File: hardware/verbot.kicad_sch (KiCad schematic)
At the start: 9 parts, among them J1 Raspberry Pi Zero 2 W, J2 5V USB power bank, M1 Pimoroni OnOff SHIM, M2 DRV8833 carrier, M3 Verbot 3V motor, M4 Verbot gearbox harness, M5 MAX98357A I2S DAC

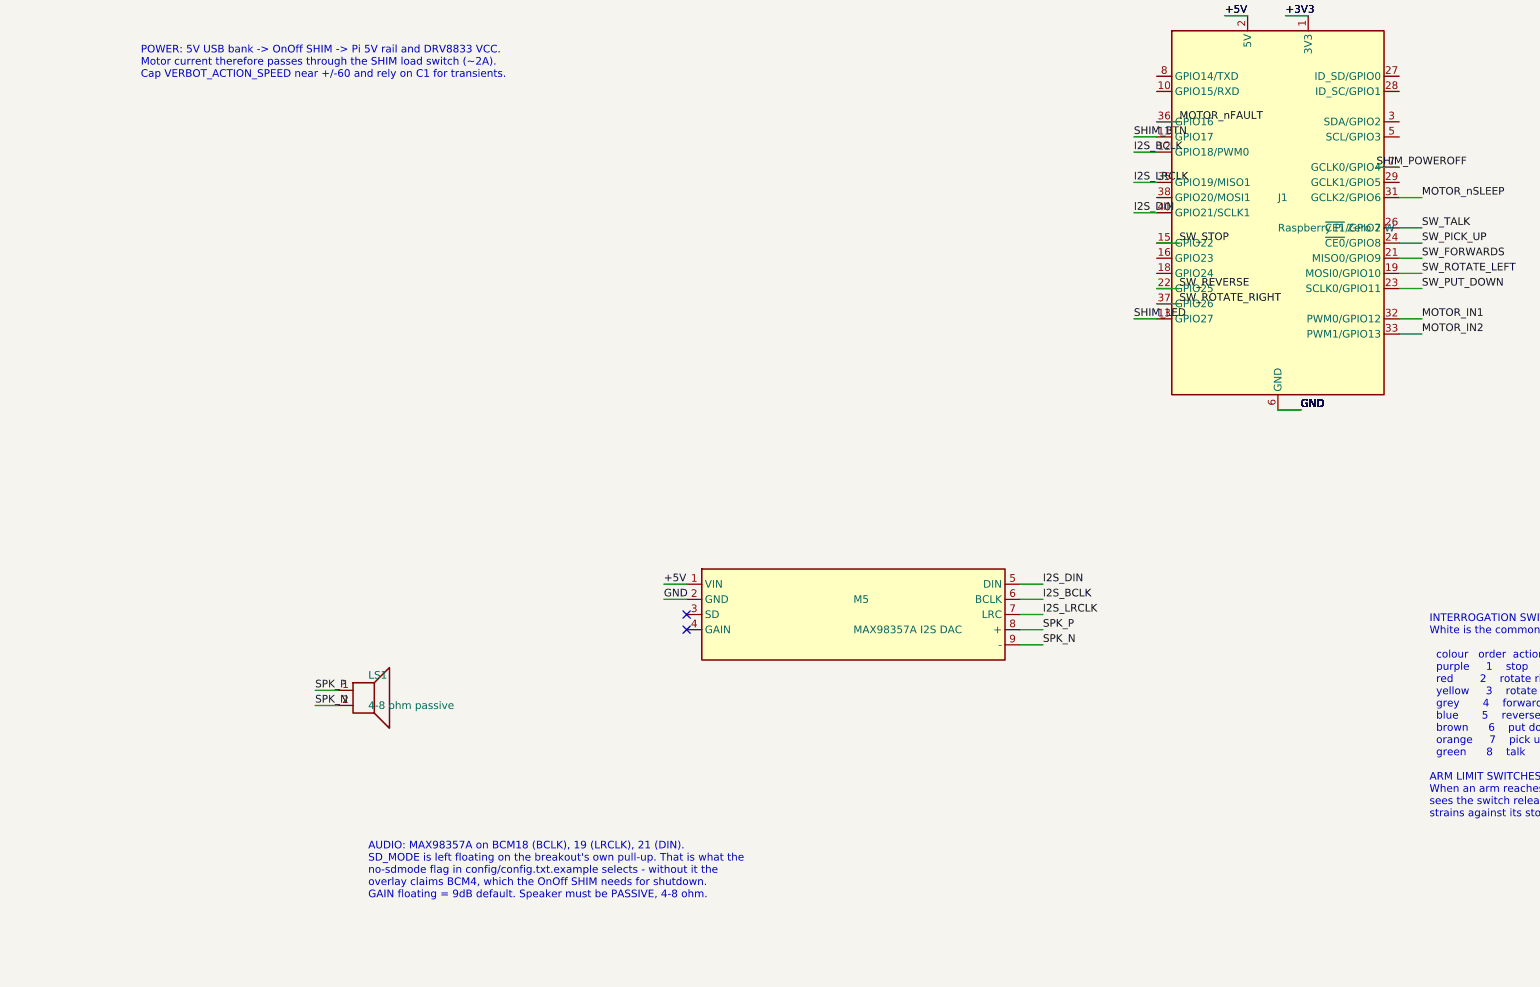
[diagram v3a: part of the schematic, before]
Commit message: feat(hardware): MCP23017 front panel, keypad and status LED
Wires an MCP23017 I2C expander (0x20, matching Settings.mcp23017_address)
to the Pi's I2C1 bus and, from it, the eight original front-panel buttons
(GPA0-7, order per BUTTON_ORDER in hardware/mcp23017.py) and a status LED
on GPB0. INTA/INTB and GPB1-7 are no-connect, matching the polling driver
and Mcp23017Led's IODIRB configuration.

Corrects the LED wiring versus the plan's assumed pin numbering:
pin_positions() shows Device:LED pin 1 is K (cathode) and pin 2 is A
(anode), the reverse of what was assumed, so the driven net is wired to
pin 2 and GND to pin 1 to avoid reverse-biasing the LED.
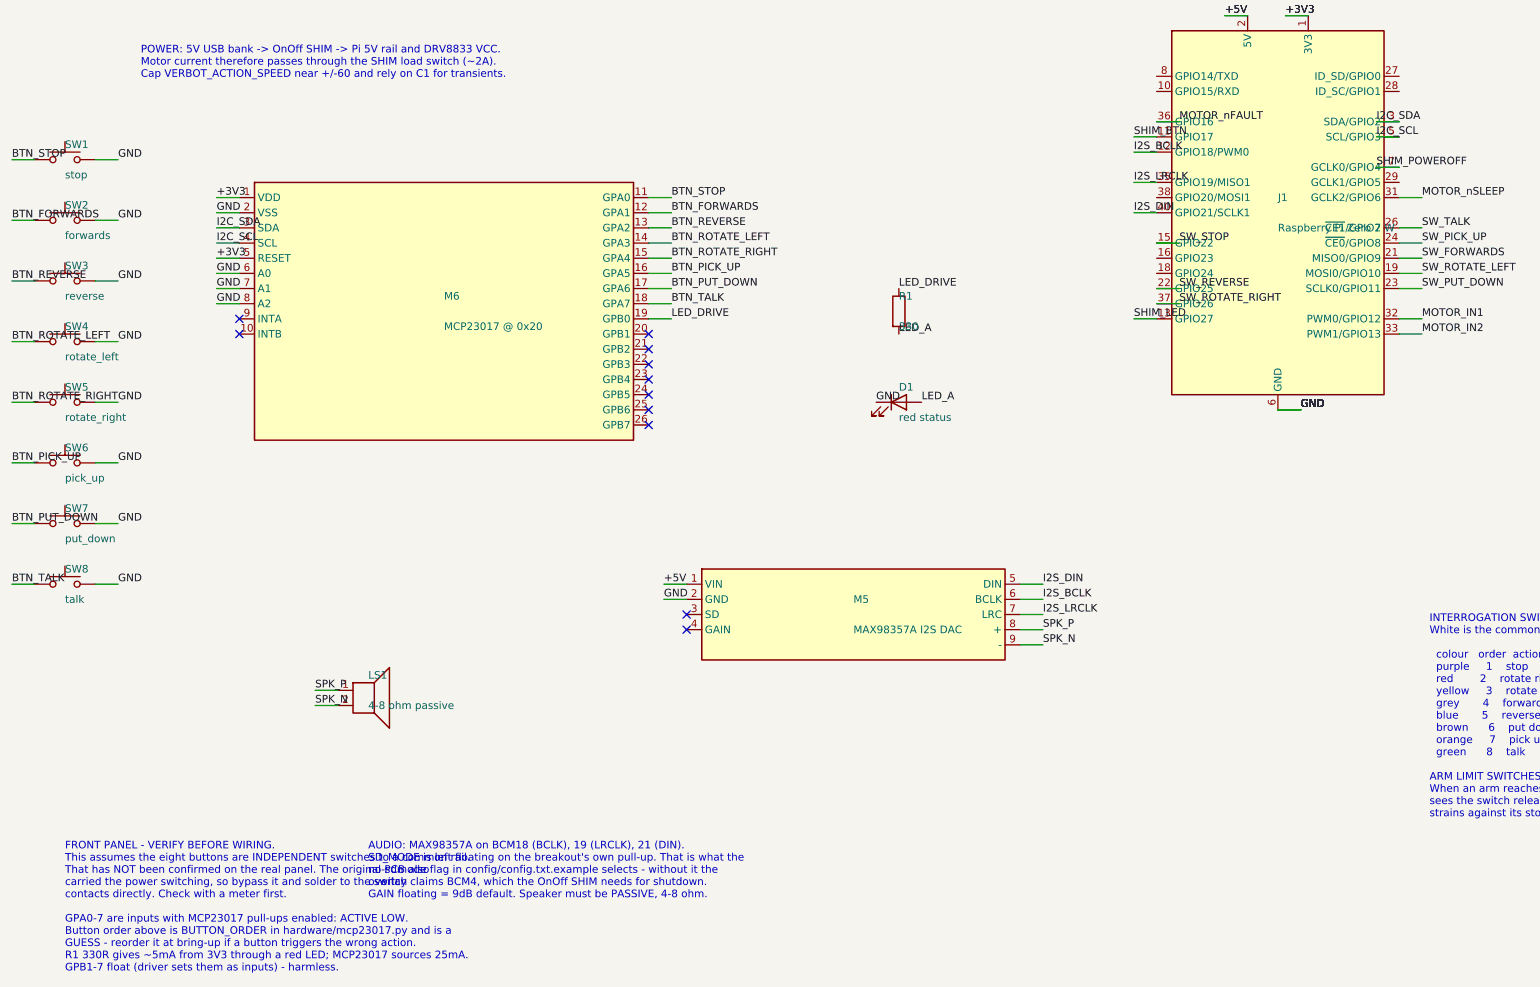
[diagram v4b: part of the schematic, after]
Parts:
- added D1: red status, symbol Device:LED
- added M6: MCP23017 @ 0x20, symbol verbot:MCP23017_Breakout
- added R1: 330, symbol Device:R
- added SW1: stop, symbol Switch:SW_Push
- added SW2: forwards, symbol Switch:SW_Push
- added SW3: reverse, symbol Switch:SW_Push
- added SW4: rotate_left, symbol Switch:SW_Push
- added SW5: rotate_right, symbol Switch:SW_Push
- added SW6: pick_up, symbol Switch:SW_Push
- added SW7: put_down, symbol Switch:SW_Push
- added SW8: talk, symbol Switch:SW_Push
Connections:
- net +3V3: now also M6.1 (VDD), M6.5 (RESET)
- net GND: now also D1.1 (K), M6.2 (VSS), M6.6 (A0), M6.7 (A1), M6.8 (A2), SW1.2, SW2.2, SW3.2, SW4.2, SW5.2, SW6.2, SW7.2, SW8.2
- net I2C_SDA: now reaches J1.3 (SDA/GPIO2)
- net I2C_SDA: now also M6.3 (SDA)
- net I2C_SCL: now reaches J1.5 (SCL/GPIO3)
- net I2C_SCL: now also M6.4 (SCL)
- new net BTN_FORWARDS: M6.12 (GPA1), SW2.1
- new net BTN_PICK_UP: M6.16 (GPA5), SW6.1
- new net BTN_PUT_DOWN: M6.17 (GPA6), SW7.1
- new net BTN_REVERSE: M6.13 (GPA2), SW3.1
- new net BTN_ROTATE_LEFT: M6.14 (GPA3), SW4.1
- new net BTN_ROTATE_RIGHT: M6.15 (GPA4), SW5.1
- new net BTN_STOP: M6.11 (GPA0), SW1.1
- new net BTN_TALK: M6.18 (GPA7), SW8.1
- new net LED_A: D1.2 (A), R1.2
- new net LED_DRIVE: M6.19 (GPB0), R1.1
- no-connect marks 10 -> 19
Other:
- note added: "FRONT PANEL - VERIFY BEFORE WIRING. This assumes the eight buttons are INDEPENDENT switches to a common rail. That has NOT been confirmed on the real panel. The original PCB also carried the power switching, so bypass it and solder to the switch contacts directly. Check with a meter first. GPA0-7 are inputs with MCP23017 pull-ups enabled: ACTIVE LOW. Button order above is BUTTON_ORDER in hardware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"

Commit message: feat(hardware): no-connect unused header pins, ERC clean
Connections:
- no-connect marks 19 -> 27
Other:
- note added: "FREE GPIO after this build: BCM 5, 14, 15, 20, 23, 24. Unused header pins carry no-connect flags so ERC stays meaningful."
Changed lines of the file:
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@@
 		(instances
 			(project "verbot"
-				(path "/16327916-eebf-4776-a795-dd11009008bb" (reference "J1") (unit 1))))
+				(path "/0445ceb6-e161-4efb-b9eb-14e73756e30d" (reference "J1") (unit 1))))
 	)
 	(symbol
@@
 		(instances
 			(project "verbot"
-				(path "/16327916-eebf-4776-a795-dd11009008bb" (reference "M1") (unit 1))))
+				(path "/0445ceb6-e161-4efb-b9eb-14e73756e30d" (reference "M1") (unit 1))))
 	)
 	(symbol
@@
 		(instances
 			(project "verbot"
-				(path "/16327916-eebf-4776-a795-dd11009008bb" (reference "J2") (unit 1))))
+				(path "/0445ceb6-e161-4efb-b9eb-14e73756e30d" (reference "J2") (unit 1))))
 	)
 	(wire (pts (xy 26.67 58.42) (xy 30.48 58.42))
@@
 		(instances
 			(project "verbot"
-				(path "/16327916-eebf-4776-a795-dd11009008bb" (reference "#FLG01") (unit 1))))
+				(path "/0445ceb6-e161-4efb-b9eb-14e73756e30d" (reference "#FLG01") (unit 1))))
 	)
 	(label "+5V" (at 44.45 105.41 0)
@@
 		(instances
 			(project "verbot"
-				(path "/16327916-eebf-4776-a795-dd11009008bb" (reference "#FLG02") (unit 1))))
+				(path "/0445ceb6-e161-4efb-b9eb-14e73756e30d" (reference "#FLG02") (unit 1))))
 	)
 	(label "+3V3" (at 69.85 105.41 0)
@@
 		(instances
 			(project "verbot"
-				(path "/16327916-eebf-4776-a795-dd11009008bb" (reference "M2") (unit 1))))
+				(path "/0445ceb6-e161-4efb-b9eb-14e73756e30d" (reference "M2") (unit 1))))
 	)
 	(symbol
@@
 		(instances
 			(project "verbot"
-				(path "/16327916-eebf-4776-a795-dd11009008bb" (reference "M3") (unit 1))))
+				(path "/0445ceb6-e161-4efb-b9eb-14e73756e30d" (reference "M3") (unit 1))))
 	)
 	(symbol
@@
 		(instances
 			(project "verbot"
-				(path "/16327916-eebf-4776-a795-dd11009008bb" (reference "C1") (unit 1))))
+				(path "/0445ceb6-e161-4efb-b9eb-14e73756e30d" (reference "C1") (unit 1))))
 	)
 	(wire (pts (xy 236.22 166.37) (xy 240.03 166.37))
@@
 		(instances
 			(project "verbot"
-				(path "/16327916-eebf-4776-a795-dd11009008bb" (reference "M4") (unit 1))))
+				(path "/0445ceb6-e161-4efb-b9eb-14e73756e30d" (reference "M4") (unit 1))))
 	)
 	(wire (pts (xy 295.91 182.88) (xy 292.1 182.88))
@@
 		(instances
 			(project "verbot"
-				(path "/16327916-eebf-4776-a795-dd11009008bb" (reference "M5") (unit 1))))
+				(path "/0445ceb6-e161-4efb-b9eb-14e73756e30d" (reference "M5") (unit 1))))
 	)
 	(symbol
@@
 		(instances
 			(project "verbot"
-				(path "/16327916-eebf-4776-a795-dd11009008bb" (reference "LS1") (unit 1))))
+				(path "/0445ceb6-e161-4efb-b9eb-14e73756e30d" (reference "LS1") (unit 1))))
 	)
 	(wire (pts (xy 116.84 210.82) (xy 113.03 210.82))
@@
 		(instances
 			(project "verbot"
-				(path "/16327916-eebf-4776-a795-dd11009008bb" (reference "M6") (unit 1))))
+				(path "/0445ceb6-e161-4efb-b9eb-14e73756e30d" (reference "M6") (unit 1))))
 	)
 	(wire (pts (xy 41.91 146.05) (xy 38.1 146.05))
@@
 		(instances
 			(project "verbot"
-				(path "/16327916-eebf-4776-a795-dd11009008bb" (reference "SW1") (unit 1))))
+				(path "/0445ceb6-e161-4efb-b9eb-14e73756e30d" (reference "SW1") (unit 1))))
 	)
 	(wire (pts (xy 7.62 139.7) (xy 3.81 139.7))
@@
 		(instances
 			(project "verbot"
-				(path "/16327916-eebf-4776-a795-dd11009008bb" (reference "SW2") (unit 1))))
+				(path "/0445ceb6-e161-4efb-b9eb-14e73756e30d" (reference "SW2") (unit 1))))
 	)
 	(wire (pts (xy 7.62 149.86) (xy 3.81 149.86))
@@
 		(instances
 			(project "verbot"
-				(path "/16327916-eebf-4776-a795-dd11009008bb" (reference "SW3") (unit 1))))
+				(path "/0445ceb6-e161-4efb-b9eb-14e73756e30d" (reference "SW3") (unit 1))))
 	)
 	(wire (pts (xy 7.62 160.02) (xy 3.81 160.02))
@@
 		(instances
 			(project "verbot"
-				(path "/16327916-eebf-4776-a795-dd11009008bb" (reference "SW4") (unit 1))))
+				(path "/0445ceb6-e161-4efb-b9eb-14e73756e30d" (reference "SW4") (unit 1))))
 	)
 	(wire (pts (xy 7.62 170.18) (xy 3.81 170.18))
@@
 		(instances
 			(project "verbot"
-				(path "/16327916-eebf-4776-a795-dd11009008bb" (reference "SW5") (unit 1))))
+				(path "/0445ceb6-e161-4efb-b9eb-14e73756e30d" (reference "SW5") (unit 1))))
 	)
 	(wire (pts (xy 7.62 180.34) (xy 3.81 180.34))
@@
 		(instances
 			(project "verbot"
-				(path "/16327916-eebf-4776-a795-dd11009008bb" (reference "SW6") (unit 1))))
+				(path "/0445ceb6-e161-4efb-b9eb-14e73756e30d" (reference "SW6") (unit 1))))
 	)
 	(wire (pts (xy 7.62 190.5) (xy 3.81 190.5))
@@
 		(instances
 			(project "verbot"
-				(path "/16327916-eebf-4776-a795-dd11009008bb" (reference "SW7") (unit 1))))
+				(path "/0445ceb6-e161-4efb-b9eb-14e73756e30d" (reference "SW7") (unit 1))))
 	)
 	(wire (pts (xy 7.62 200.66) (xy 3.81 200.66))
@@
 		(instances
 			(project "verbot"
-				(path "/16327916-eebf-4776-a795-dd11009008bb" (reference "SW8") (unit 1))))
+				(path "/0445ceb6-e161-4efb-b9eb-14e73756e30d" (reference "SW8") (unit 1))))
 	)
 	(wire (pts (xy 7.62 210.82) (xy 3.81 210.82))
@@
 		(instances
 			(project "verbot"
-				(path "/16327916-eebf-4776-a795-dd11009008bb" (reference "R1") (unit 1))))
+				(path "/0445ceb6-e161-4efb-b9eb-14e73756e30d" (reference "R1") (unit 1))))
 	)
 	(symbol
@@
 		(instances
 			(project "verbot"
-				(path "/16327916-eebf-4776-a795-dd11009008bb" (reference "D1") (unit 1))))
+				(path "/0445ceb6-e161-4efb-b9eb-14e73756e30d" (reference "D1") (unit 1))))
 	)
 	(wire (pts (xy 110.49 166.37) (xy 114.3 166.37))
@@
 	(text "FRONT PANEL - VERIFY BEFORE WIRING.\nThis assumes the eight buttons are INDEPENDENT switches to a common rail.\nThat has NOT been confirmed on the real panel. The original PCB also\ncarried the power switching, so bypass it and solder to the switch\ncontacts directly. Check with a meter first.\n\nGPA0-7 are inputs with MCP23017 pull-ups enabled: ACTIVE LOW.\nButton order above is BUTTON_ORDER in hardware/mcp23017.py and is a\nGUESS - reorder it at bring-up if a button triggers the wrong action.\nR1 330R gives ~5mA from 3V3 through a red LED; MCP23017 sources 25mA.\nGPB1-7 float (driver sets them as inputs) - harmless." (at 12.7 254.0 0)
 		(effects (font (size 1.27 1.27)) (justify left top)))
+	(no_connect (at 195.58 125.73))
+	(no_connect (at 195.58 128.27))
+	(no_connect (at 195.58 156.21))
+	(no_connect (at 195.58 158.75))
+	(no_connect (at 236.22 125.73))
+	(no_connect (at 236.22 128.27))
+	(no_connect (at 236.22 143.51))
+	(no_connect (at 195.58 146.05))
+	(text "FREE GPIO after this build: BCM 5, 14, 15, 20, 23, 24.\nUnused header pins carry no-connect flags so ERC stays meaningful." (at 215.9 254.0 0)
+		(effects (font (size 1.27 1.27)) (justify left top)))
 	(sheet_instances
